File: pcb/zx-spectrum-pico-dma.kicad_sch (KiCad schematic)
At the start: 19 parts, among them J101 SWD, J102 Blippers, J103 Z80 Data Bus, J104 Z80 Address Bus, J105 Z80 Control Bus, J106 ZX Control, J107 OLED, J108 Spare GPIOs, Q101 PMBT2222A, SW101 BTN_RESET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

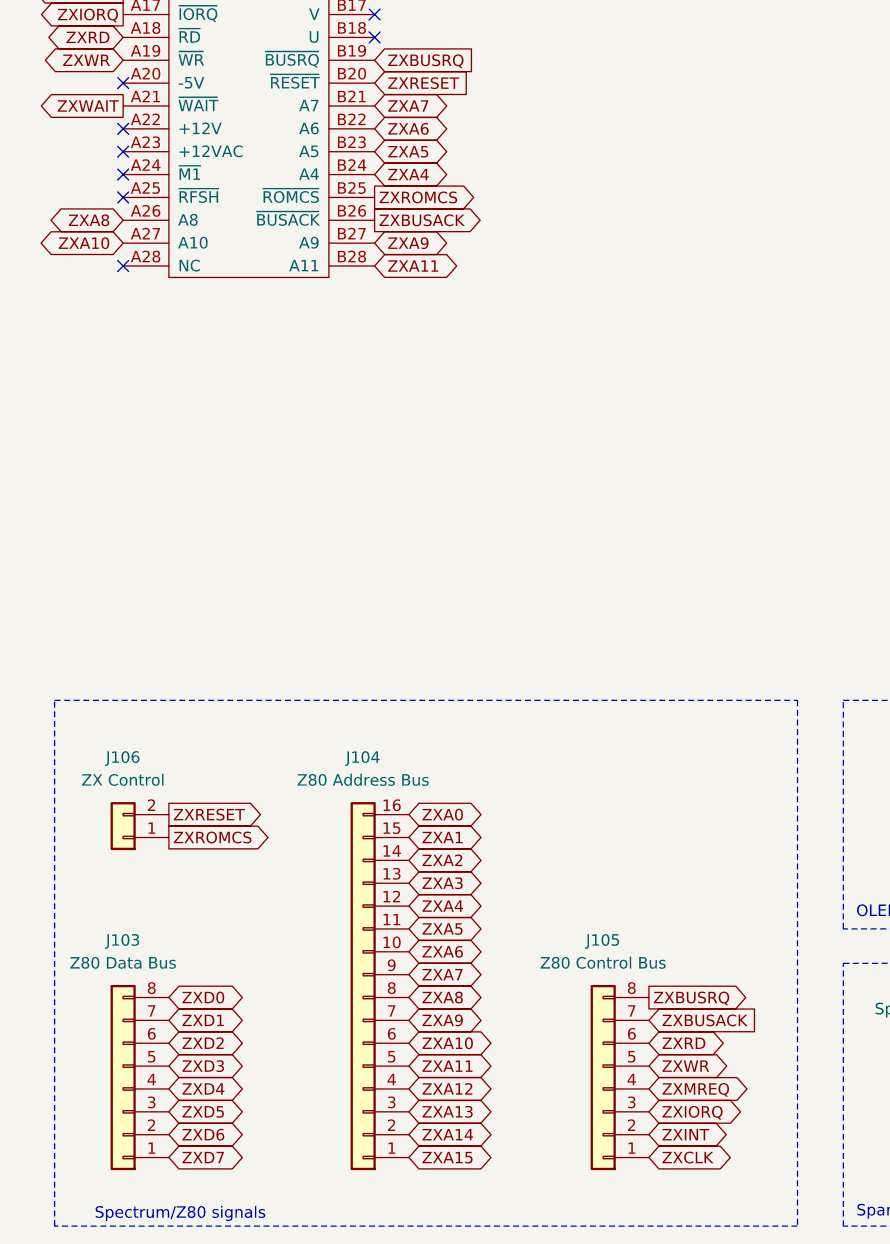
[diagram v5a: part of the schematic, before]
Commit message: add M1 from edge connector to a pin, it's needed on the logic analyser so I need to make it available
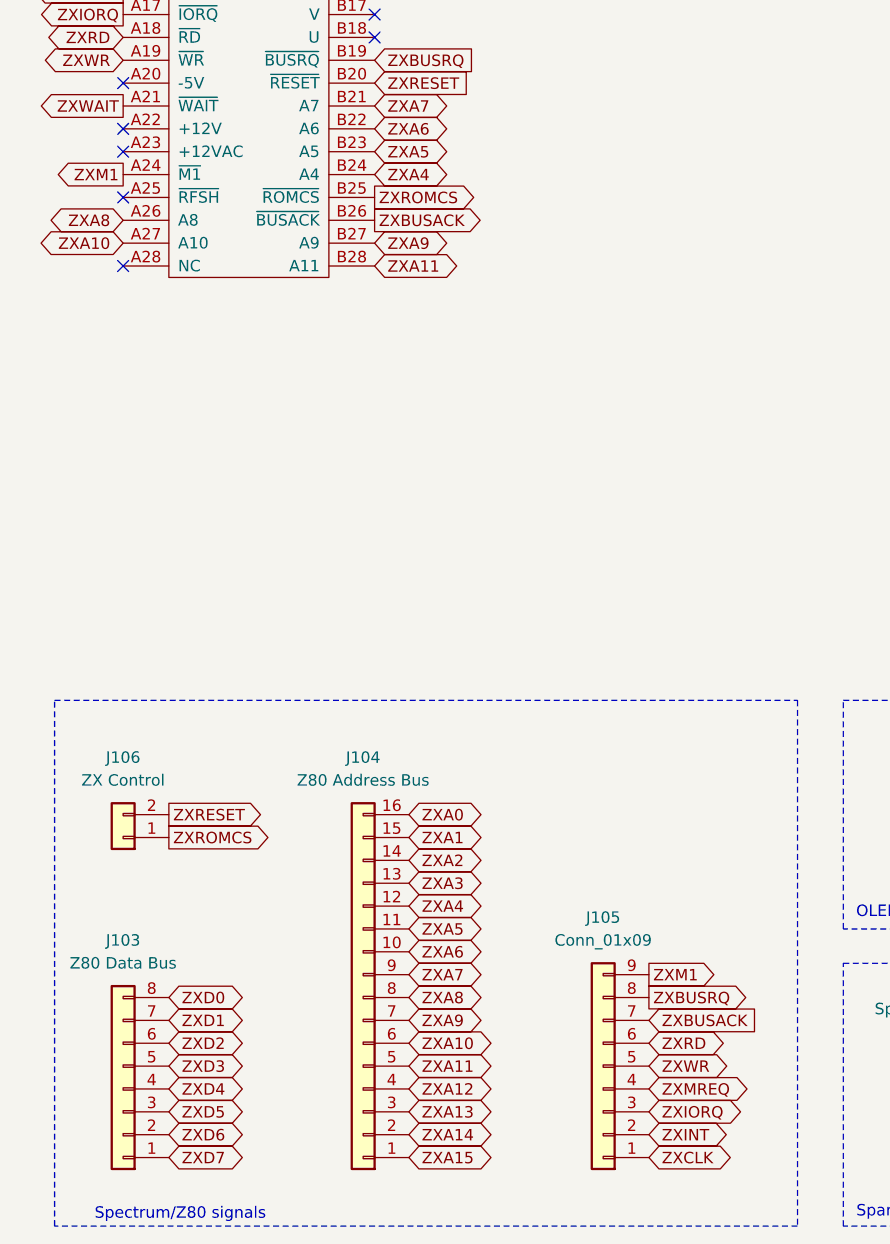
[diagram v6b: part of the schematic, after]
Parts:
- removed J105: Z80 Control Bus, Connector_PinHeader_2.54mm:PinHeader_1x08_P2.54mm_Vertical, symbol Connector_Generic:Conn_01x08
- added J105: Conn_01x09, Connector_PinHeader_2.54mm:PinHeader_1x09_P2.54mm_Vertical, symbol Connector_Generic:Conn_01x09
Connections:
- net ZXBUSACK: now also J105.7 (Pin_7)
- net ZXBUSRQ: now also J105.8 (Pin_8)
- net ZXCLK: now also J105.1 (Pin_1)
- net ZXINT: now also J105.2 (Pin_2)
- net ZXIORQ: now also J105.3 (Pin_3)
- net ZXMREQ: now also J105.4 (Pin_4)
- net ZXRD: now also J105.6 (Pin_6)
- net ZXWR: now also J105.5 (Pin_5)
- net ZXM1: now reaches Z101.A24 (~{M1})
- net ZXM1: now also J105.9 (Pin_9)
- no-connect marks 20 -> 19
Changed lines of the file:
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@@
 	(title_block
 		(title "RP2350B Spectrum DMA Interface")
-		(date "2025-02-26")
+		(date "2025-03-14")
 	)
 	(junction
@@
 	)
 	(no_connect
-		(at 26.67 80.01)
-	)
-	(no_connect
 		(at 26.67 74.93)
 	)
@@
 		)
 	)
+	(global_label "ZXM1"
+		(shape output)
+		(at 85.09 168.91 0)
+		(fields_autoplaced yes)
+		(effects
+			(font
+				(size 1.27 1.27)
+			)
+			(justify left)
+		)
+		(property "Intersheetrefs" "${INTERSHEET_REFS}"
+			(at 93.1551 168.91 0)
+			(effects
+				(font
+					(size 1.27 1.27)
+				)
+				(justify left)
+				(hide yes)
+			)
+		)
+	)
+	(global_label "ZXM1"
+		(shape output)
+		(at 26.67 80.01 180)
+		(fields_autoplaced yes)
+		(effects
+			(font
+				(size 1.27 1.27)
+			)
+			(justify right)
+		)
+		(property "Intersheetrefs" "${INTERSHEET_REFS}"
+			(at 18.6049 80.01 0)
+			(effects
+				(font
+					(size 1.27 1.27)
+				)
+				(justify right)
+				(hide yes)
+			)
+		)
+	)
 	(global_label "ZXA4"
 		(shape bidirectional)
@@
 	)
 	(symbol
-		(lib_id "power:GND")
-		(at 143.51 152.4 0)
+		(lib_id "Connector_Generic:Conn_01x09")
+		(at 80.01 179.07 180)
 		(unit 1)
 		(exclude_from_sim no)
@@
 		(dnp no)
 		(fields_autoplaced yes)
-		(property "Reference" "#PWR0108"
-			(at 143.51 158.75 0)
+		(property "Reference" "J105"
+			(at 80.01 162.56 0)
 			(effects
 				(font
 					(size 1.27 1.27)
 				)
-				(hide yes)
 			)
 		)
-		(property "Value" "GND"
-			(at 143.51 157.48 0)
+		(property "Value" "Conn_01x09"
+			(at 80.01 165.1 0)
 			(effects
 				(font
@@
 			)
 		)
-		(property "Footprint" ""
-			(at 143.51 152.4 0)
+		(property "Footprint" "Connector_PinHeader_2.54mm:PinHeader_1x09_P2.54mm_Vertical"
+			(at 80.01 179.07 0)
 			(effects
 				(font
@@
 			)
 		)
-		(property "Datasheet" ""
-			(at 143.51 152.4 0)
+		(property "Datasheet" "~"
+			(at 80.01 179.07 0)
 			(effects
 				(font
@@
 			)
 		)
-		(property "Description" "Power symbol creates a global label with name \"GND\" , ground"
-			(at 143.51 152.4 0)
+		(property "Description" "Generic connector, single row, 01x09, script generated (kicad-library-utils/schlib/autogen/connector/)"
+			(at 80.01 179.07 0)
 			(effects
 				(font
@@
 			)
 		)
+		(pin "5"
+		)
 		(pin "1"
 		)
+		(pin "4"
+		)
+		(pin "3"
+		)
+		(pin "2"
+		)
+		(pin "6"
+		)
+		(pin "9"
+		)
+		(pin "7"
+		)
+		(pin "8"
+		)
 		(instances
 			(project ""
 				(path "/d8e2427c-cc3d-4679-b4b6-2ba21d9ca0ef"
-					(reference "#PWR0108")
+					(reference "J105")
 					(unit 1)
 				)
@@
 	)
 	(symbol
-		(lib_id "Connector_Generic:Conn_01x08")
-		(at 80.01 181.61 180)
+		(lib_id "power:GND")
+		(at 143.51 152.4 0)
 		(unit 1)
 		(exclude_from_sim no)
@@
 		(dnp no)
 		(fields_autoplaced yes)
-		(property "Reference" "J105"
-			(at 80.01 165.1 0)
+		(property "Reference" "#PWR0108"
+			(at 143.51 158.75 0)
 			(effects
 				(font
 					(size 1.27 1.27)
 				)
+				(hide yes)
 			)
 		)
-		(property "Value" "Z80 Control Bus"
-			(at 80.01 167.64 0)
+		(property "Value" "GND"
+			(at 143.51 157.48 0)
 			(effects
 				(font
@@
 			)
 		)
-		(property "Footprint" "Connector_PinHeader_2.54mm:PinHeader_1x08_P2.54mm_Vertical"
-			(at 80.01 181.61 0)
+		(property "Footprint" ""
+			(at 143.51 152.4 0)
 			(effects
 				(font
@@
 			)
 		)
-		(property "Datasheet" "~"
-			(at 80.01 181.61 0)
+		(property "Datasheet" ""
+			(at 143.51 152.4 0)
 			(effects
 				(font
@@
 			)
 		)
-		(property "Description" "Generic connector, single row, 01x08, script generated (kicad-library-utils/schlib/autogen/connector/)"
-			(at 80.01 181.61 0)
+		(property "Description" "Power symbol creates a global label with name \"GND\" , ground"
+			(at 143.51 152.4 0)
 			(effects
 				(font
@@
 		(pin "1"
 		)
-		(pin "7"
-		)
-		(pin "3"
-		)
-		(pin "4"
-		)
-		(pin "2"
-		)
-		(pin "5"
-		)
-		(pin "6"
-		)
-		(pin "8"
-		)
 		(instances
 			(project ""
 				(path "/d8e2427c-cc3d-4679-b4b6-2ba21d9ca0ef"
-					(reference "J105")
+					(reference "#PWR0108")
 					(unit 1)
 				)

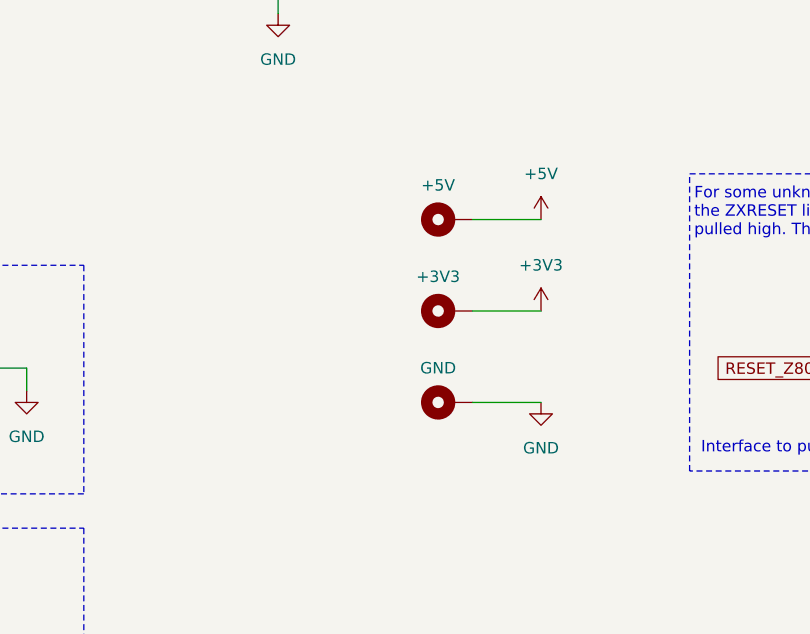
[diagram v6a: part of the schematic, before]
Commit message: add a 3-pin supplies header, the mounting points aren't easy to attach a clip to
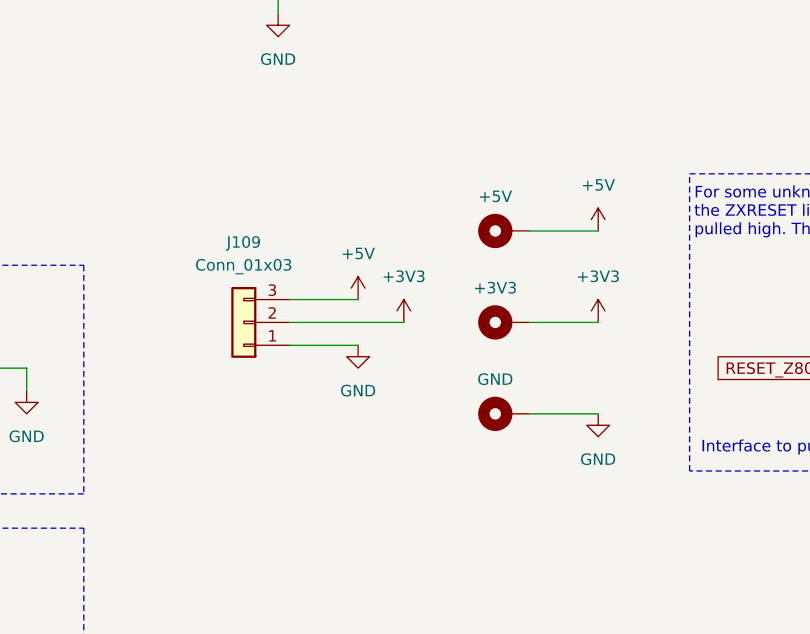
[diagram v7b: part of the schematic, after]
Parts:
- added J109: Conn_01x03, Connector_PinHeader_2.54mm:PinHeader_1x03_P2.54mm_Vertical, symbol Connector_Generic:Conn_01x03
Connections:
- net +3V3: now also J109.2 (Pin_2)
- net +5V: now also J109.3 (Pin_3)
- net GND: now also J109.1 (Pin_1)
